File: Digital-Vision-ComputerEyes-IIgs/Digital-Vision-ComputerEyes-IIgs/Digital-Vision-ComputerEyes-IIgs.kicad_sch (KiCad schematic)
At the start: 59 parts, among them U10 NE5037, U11 74LS155, U12 74HCT4066, U13 GL324, U2 LM556, U3 74LS04, U4 74HCT4066, U5 74HCT4066, U6 GL324, U8 74LS273, U9 74LS244

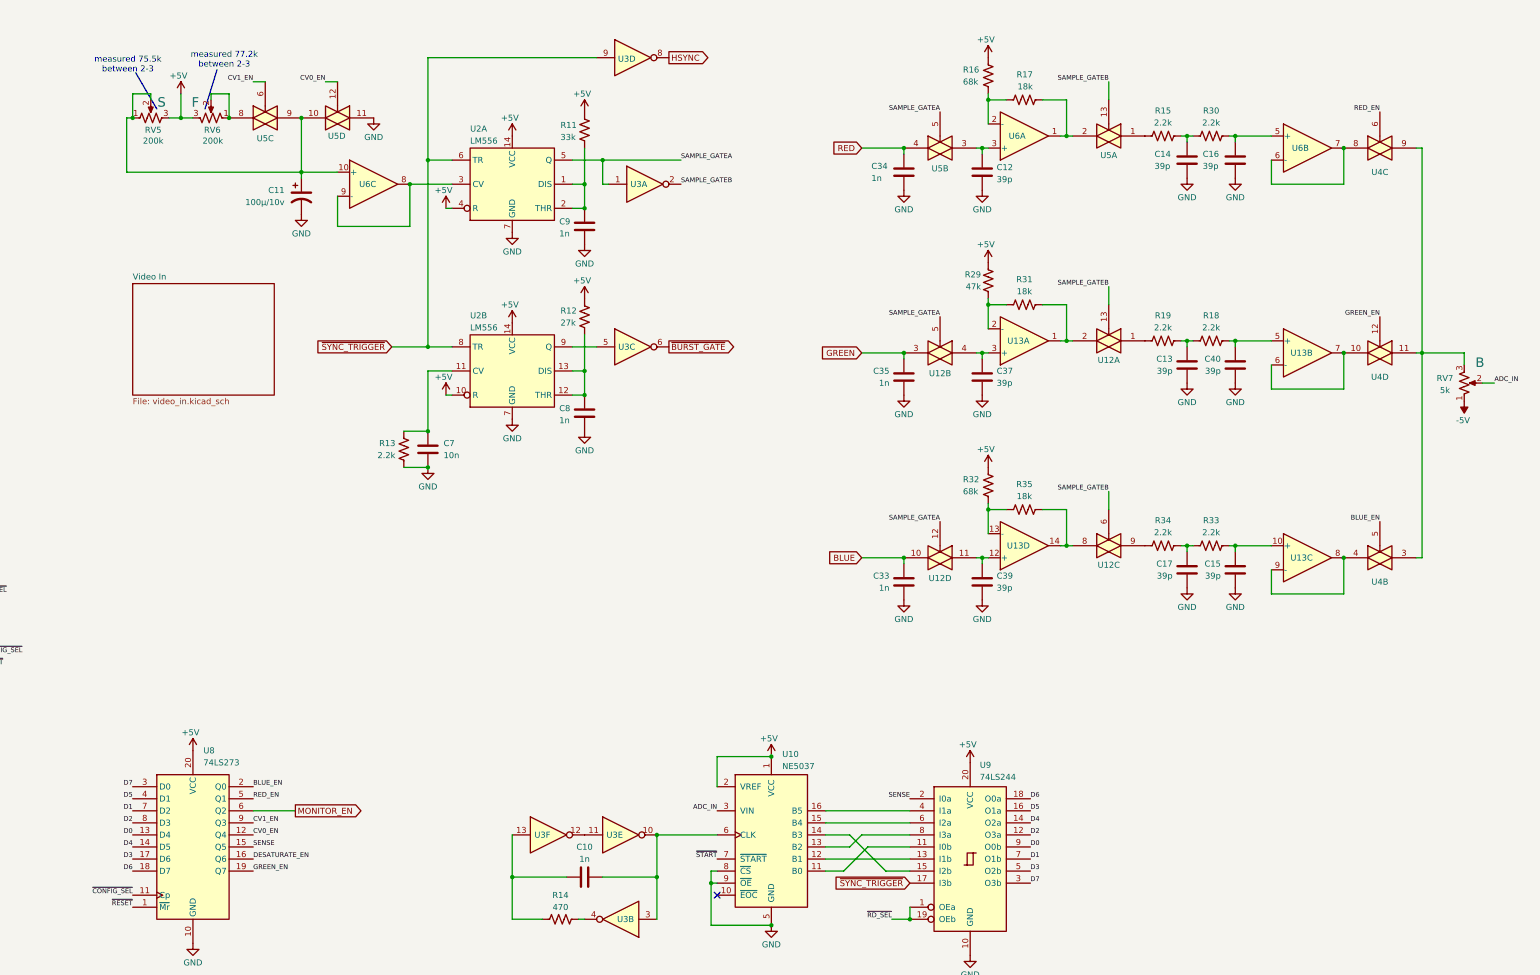
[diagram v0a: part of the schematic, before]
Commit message: Add some more details on ComputerEyes operation
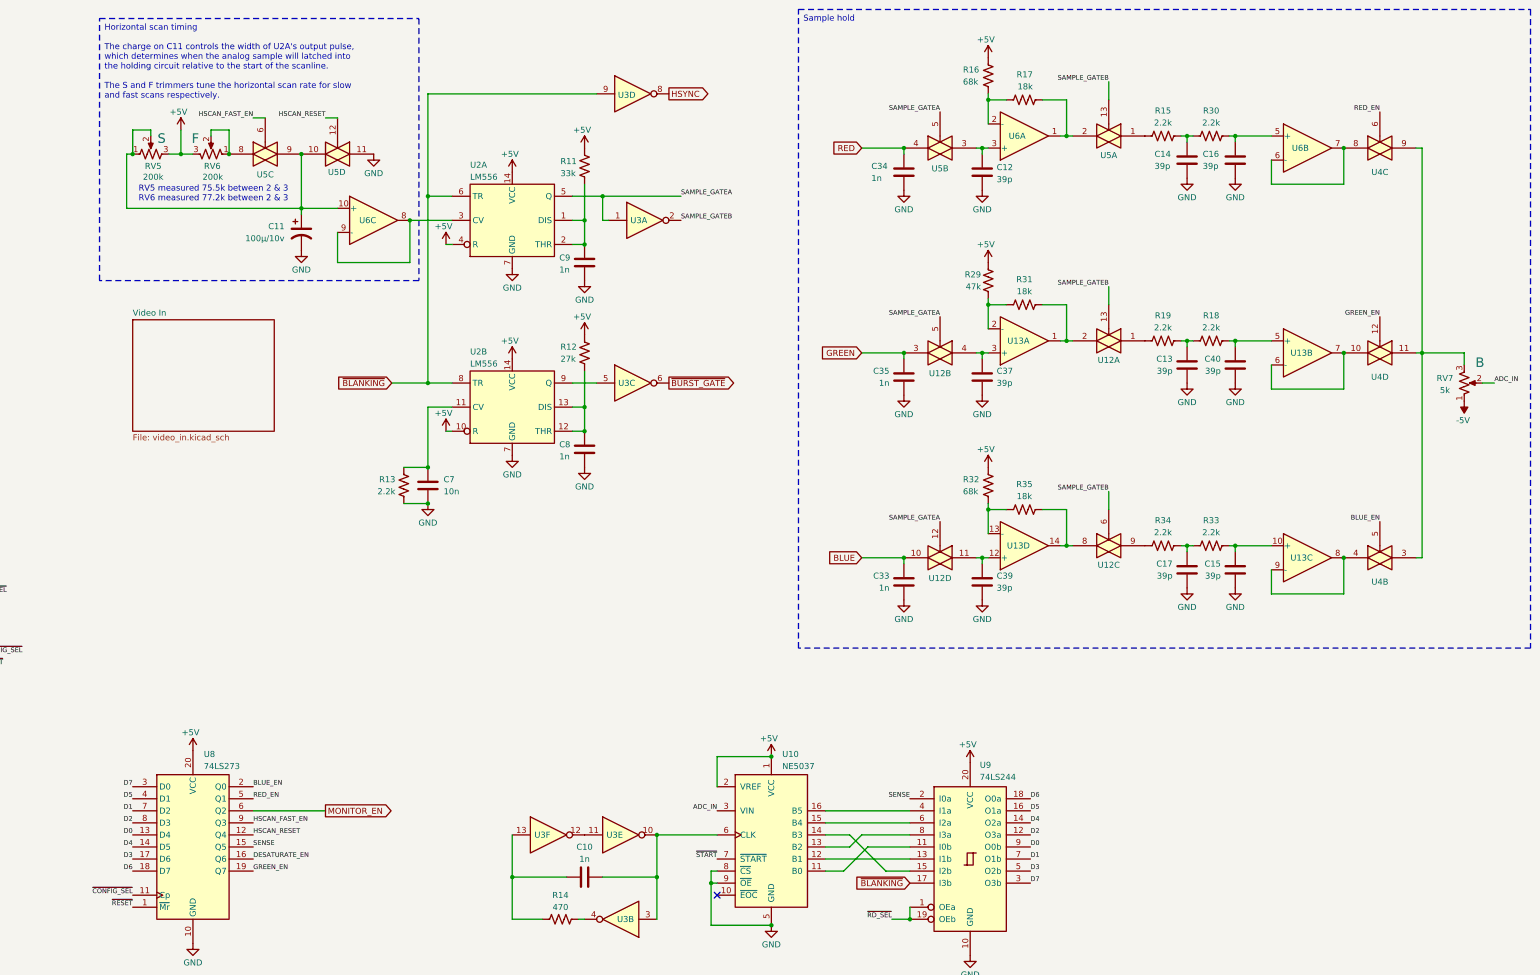
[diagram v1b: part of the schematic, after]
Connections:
- net CV0_EN renamed HSCAN_RESET
- net CV1_EN renamed HSCAN_FAST_EN
- net ~{SYNC_TRIGGER} renamed ~{BLANKING}
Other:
- note added: "RV5 measured 75.5k between 2 & 3 RV6 measured 77.2k between 2 & 3"
- note removed: "measured 75.5k between 2-3"
- note removed: "measured 77.2k between 2-3"
- moved on the sheet: C11, C7, C8, C9, R11, R12, R13, RV5, RV6, U2A, U2B, U3A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
